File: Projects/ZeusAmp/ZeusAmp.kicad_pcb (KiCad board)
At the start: 2 copper layers, 58 parts, among them Q1 NZT660, Q11 NZT660, Q12 NZT660, Q121 NZT660, Q2 NZT660, Q21 NZT660, Q3 PZTA06, Q31 PZTA06, Q4 MJD340T4, Q41 MJD340T4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

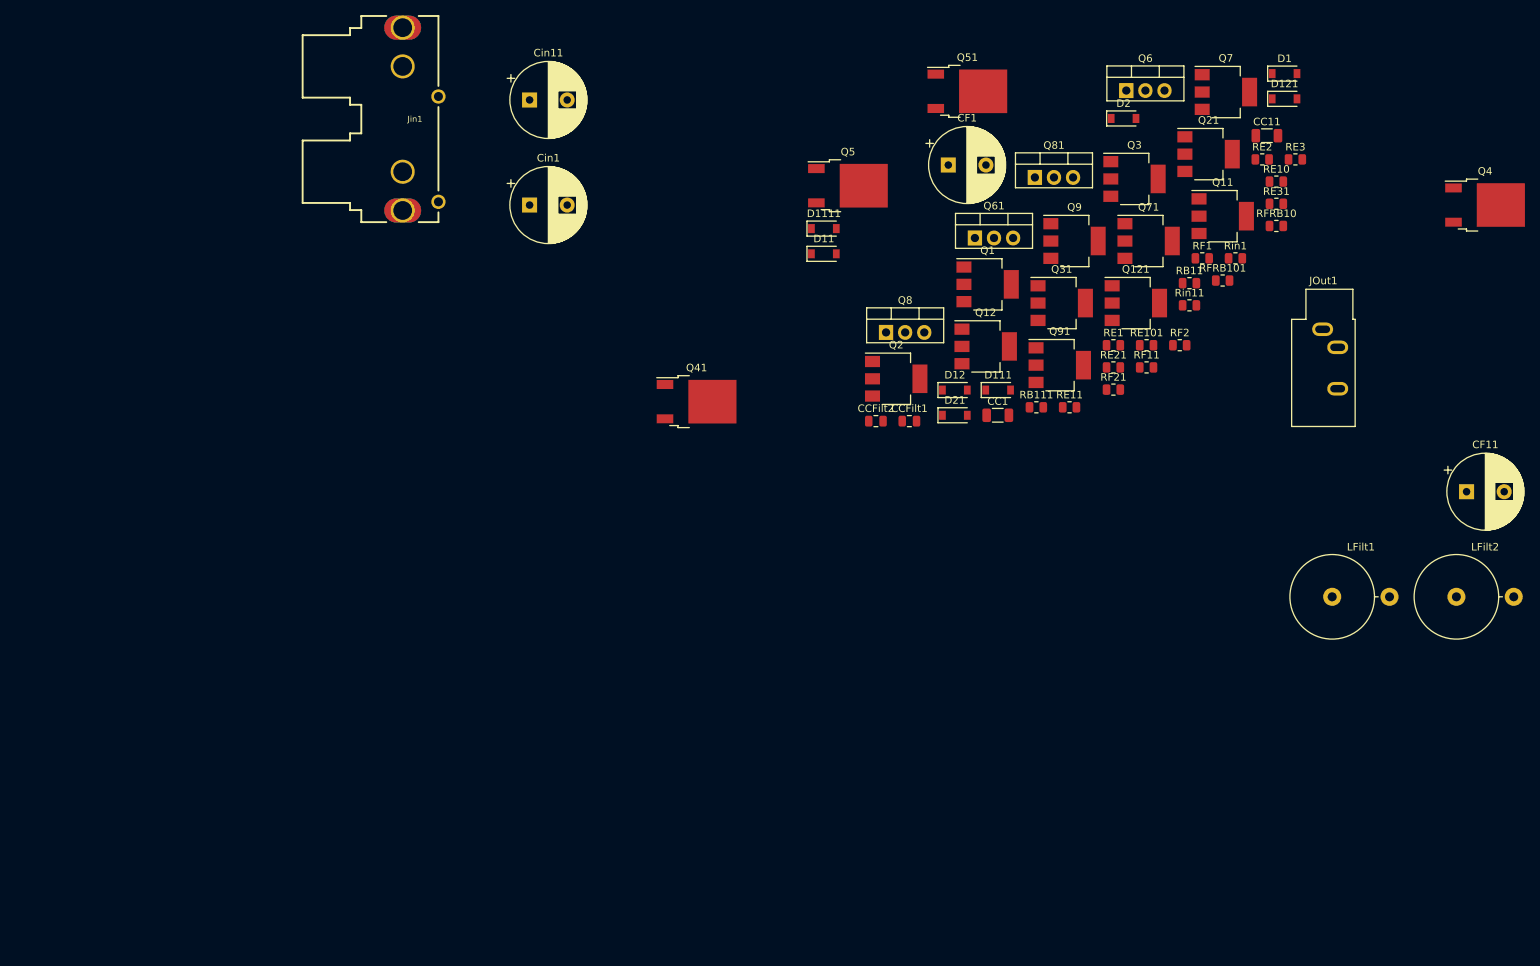
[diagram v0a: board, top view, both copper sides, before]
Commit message: completed full layout, needs volume control pot and +-15V rails
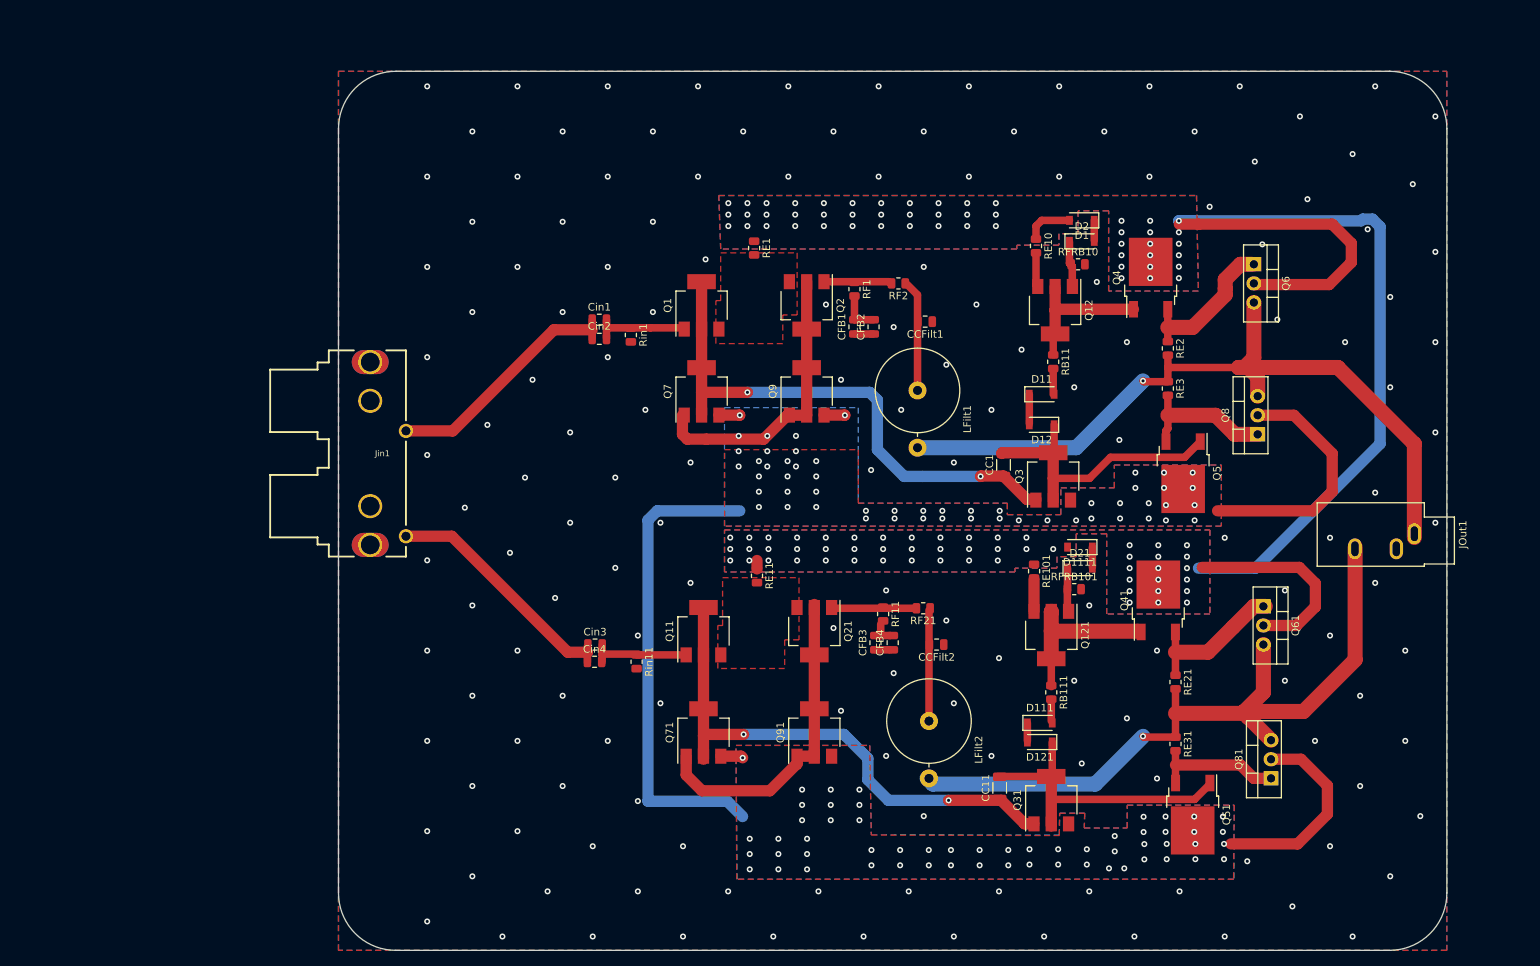
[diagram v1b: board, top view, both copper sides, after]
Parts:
- removed CF1, CF11, Cin11: 20u, Capacitor_THT:CP_Radial_D10.0mm_P5.00mm
- added CFB1: 10u, Capacitor_SMD:C_0805_2012Metric, F.Cu at (127.0, 84.8)
- added CFB2: 10u, Capacitor_SMD:C_0805_2012Metric, F.Cu at (129.5, 84.8)
- added CFB3: 10u, Capacitor_SMD:C_0805_2012Metric, F.Cu at (129.8, 126.7)
- added CFB4: 10u, Capacitor_SMD:C_0805_2012Metric, F.Cu at (132.1, 126.7)
- added Cin2: 10u, Capacitor_SMD:C_0805_2012Metric, F.Cu at (93.1, 86.4)
- added Cin3: 10u, Capacitor_SMD:C_0805_2012Metric, F.Cu at (92.5, 127.0)
- added Cin4: 10u, Capacitor_SMD:C_0805_2012Metric, F.Cu at (92.5, 129.3)
- Cin1: value 20u -> 10u; footprint Capacitor_THT:CP_Radial_D10.0mm_P5.00mm -> Capacitor_SMD:C_0805_2012Metric
- moved Q51 100.7 mm to (172.0, 149.6), turned to 270 degrees
- moved CC11 93.7 mm to (146.3, 146.1), turned to 90 degrees
- moved D121 91.5 mm to (151.6, 140.0), turned to 180 degrees
- moved Q11 88.4 mm to (106.9, 125.2), turned to 90 degrees
- moved Q71 88.1 mm to (106.9, 138.7), turned to 90 degrees
- moved Rin11 87.4 mm to (98.0, 129.3), turned to 270 degrees
- moved Q81 85.8 mm to (182.4, 144.8), turned to 90 degrees
- moved Q21 82.3 mm to (121.7, 125.2), turned to 270 degrees
- moved Rin1 81.0 mm to (97.3, 85.9), turned to 270 degrees
- moved Q7 80.2 mm to (106.7, 93.3), turned to 90 degrees
- moved RE31 73.0 mm to (169.7, 140.2), turned to 270 degrees
- moved LFilt2 72.0 mm to (136.9, 137.2), turned to 270 degrees
- moved Q41 66.8 mm to (167.4, 121.1), turned to 90 degrees
- moved Q31 66.1 mm to (153.2, 147.7), turned to 90 degrees
- moved Q61 62.2 mm to (181.4, 121.9), turned to 270 degrees
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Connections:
- net Net-(Q1-Pad3) renamed /CollectorInput
- Jin1 pad 2: Net-(Cin11-Pad1) -> Net-(Cin1-Pad1)
- Jin1 pad 4: Net-(Cin1-Pad1) -> Net-(Cin3-Pad1)
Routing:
- net /VCC: track 0.00 -> 164.3 mm, vias 0 -> 105
- net /VEE: track 0.00 -> 132.6 mm, vias 0 -> 102
- net /LeftAudioChannel: track 0.00 -> 105.4 mm, vias 0 -> 1
- net /RightAudioChannel: track 0.00 -> 100.5 mm, vias 0 -> 1
- net Net-(CC1-Pad1): track 0.00 -> 72.0 mm, vias 0 -> 2
- net Net-(CC11-Pad1): track 0.00 -> 70.8 mm, vias 0 -> 2
- net Net-(Q21-Pad2): track 0.00 -> 42.0 mm
- net Net-(CC11-Pad2): track 0.00 -> 40.2 mm
- net Net-(CC1-Pad2): track 0.00 -> 38.8 mm
- net Net-(Q2-Pad2): track 0.00 -> 38.4 mm, vias 0 -> 2
- net Net-(Cin1-Pad1): track 0.00 -> 32.8 mm
- net Net-(Cin3-Pad1): track 0.00 -> 32.6 mm
- net Net-(Q121-Pad2): track 0.00 -> 21.3 mm
- net Net-(Q4-Pad3): track 0.00 -> 20.0 mm
- net Net-(Q41-Pad3): track 0.00 -> 19.9 mm
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- added copper zone on F.Cu, net /CollectorInput
- added copper zone on B.Cu, net /VCC
- added copper zone on F.Cu, net /VCC
- added copper zone on B.Cu, net /VEE
- added copper zone on F.Cu, net /VEE
- added copper zone on B.Cu, net GND
- added copper zone on F.Cu, net GND
- added copper zone on F.Cu, net Net-(Q11-Pad3)
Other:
- board outline added: 147.3 x 116.8 mm

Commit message: First Zeus V1 completed
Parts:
- added 16VACIn1: Barrel_Jack, Connector_BarrelJack:BarrelJack_Horizontal, F.Cu at (33.0, 134.6)
- added CPower1: 1000u, Capacitor_THT:CP_Radial_D13.0mm_P5.00mm, F.Cu at (46.2, 128.8)
- added CPower11: 1000u, Capacitor_THT:CP_Radial_D13.0mm_P5.00mm, F.Cu at (45.7, 160.0)
- added CPower2: 10u, Capacitor_SMD:C_0805_2012Metric, F.Cu at (51.6, 134.9)
- added CPower22: 10u, Capacitor_Tantalum_SMD:CP_EIA-6032-28_Kemet-C, F.Cu at (55.1, 148.6)
- added CPower3: 10u, Capacitor_Tantalum_SMD:CP_EIA-6032-28_Kemet-C, F.Cu at (73.7, 133.7)
- added CPower5: 10u, Capacitor_Tantalum_SMD:CP_EIA-6032-28_Kemet-C, F.Cu at (78.7, 157.5)
- added DP1: 1N4148W, Diode_SMD:D_SOD-123, F.Cu at (43.2, 146.3)
- added DP2: 1N4148W, Diode_SMD:D_SOD-123, F.Cu at (44.5, 135.9)
- added RV1: R_POT_Dual, Potentiometer_THT:Potentiometer_Alps_RK09L_Double_Vertical, F.Cu at (85.2, 106.3)
- added U5: LM2990S-15_NOPB, Package_TO_SOT_SMD:TO-263-3_TabPin2, F.Cu at (66.0, 149.6)
- added U6: LM2937ESX-15_NOPB, Package_TO_SOT_SMD:TO-263-3_TabPin2, F.Cu at (61.4, 130.4)
- moved Jin1 33.8 mm to (30.5, 101.6)
- moved Cin4 13.0 mm to (91.4, 116.3)
- moved Rin11 13.0 mm to (97.0, 116.3)
- moved Cin3 13.0 mm to (91.5, 114.0)
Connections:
- Jin1 pad 2: Net-(Cin1-Pad1) -> Net-(Jin1-Pad2)
- Jin1 pad 4: Net-(Cin3-Pad1) -> Net-(Jin1-Pad4)
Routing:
- net /VCC: track 164.3 -> 281.6 mm, vias 105 -> 106
- net Net-(Jin1-Pad2): track 0.00 -> 55.9 mm
- net Net-(Jin1-Pad4): track 0.00 -> 52.5 mm
- net /VEE: track 132.6 -> 179.5 mm
- net Net-(CPower11-Pad2): track 0.00 -> 40.6 mm
- net /V-: track 0.00 -> 27.0 mm
- net Net-(CPower1-Pad1): track 0.00 -> 19.7 mm
- net /V+: track 0.00 -> 10.1 mm
- net Net-(Cin3-Pad2): track 13.4 -> 23.2 mm
- net Net-(Cin3-Pad1): track 32.6 -> 23.6 mm, vias 0 -> 1
- net GND: track 4.50 -> 13.5 mm, vias 159 -> 143
- net Net-(Cin1-Pad1): track 32.8 -> 24.2 mm
- net Net-(Q2-Pad2): vias 2 -> 0
- net (no net): vias 7 -> 0
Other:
- board size 147.3 x 116.8 mm -> 182.9 x 104.1 mm

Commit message: Fixed Power Supply Issue
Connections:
- 16VACIn1 pad 2: /V- -> GND
- DP1 pad 1: /V- -> /V+
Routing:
- net /V-: track 27.0 -> 0.00 mm
- net /V+: track 10.1 -> 23.8 mm

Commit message: Added Drill holes
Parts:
- added H1: MountingHole_Pad, MountingHole:MountingHole_2.2mm_M2, F.Cu at (30.5, 71.1)
- added H2: MountingHole_Pad, MountingHole:MountingHole_2.2mm_M2, F.Cu at (198.1, 71.1)
- added H3: MountingHole_Pad, MountingHole:MountingHole_2.2mm_M2, F.Cu at (198.1, 160.0)
- added H4: MountingHole_Pad, MountingHole:MountingHole_2.2mm_M2, F.Cu at (30.5, 160.0)
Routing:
- net /VCC: track 281.6 -> 271.9 mm
- net GND: vias 143 -> 139
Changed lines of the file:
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@@
     (thickness 1.6)
     (drawings 8)
-    (tracks 630)
+    (tracks 623)
     (zones 0)
-    (modules 74)
+    (modules 78)
     (nets 45)
   )
@@
   )
   (setup
-    (last_trace_width 0.5)
+    (last_trace_width 2)
     (user_trace_width 0.5)
     (user_trace_width 1)
@@
     (add_net "Net-(Q51-Pad3)")
   )
+  (module MountingHole:MountingHole_2.2mm_M2 (layer F.Cu)
+    (at 30.48 160.02)
+    (descr "Mounting Hole 2.2mm, no annular, M2")
+    (tags "mounting hole 2.2mm no annular m2")
+    (attr virtual)
+    (fp_text reference H4 (at 0 -3.2) (layer F.SilkS)
+      (effects (font (size 1 1) (thickness 0.15)))
+    )
+    (fp_text value MountingHole_Pad (at 0 3.2) (layer F.Fab)
+      (effects (font (size 1 1) (thickness 0.15)))
+    )
+    (fp_text user %R (at 0.3 0) (layer F.Fab)
+      (effects (font (size 1 1) (thickness 0.15)))
+    )
+    (fp_circle (center 0 0) (end 2.2 0) (layer Cmts.User) (width 0.15))
+    (fp_circle (center 0 0) (end 2.45 0) (layer F.CrtYd) (width 0.05))
+    (pad 1 np_thru_hole circle (at 0 0) (size 2.2 2.2) (drill 2.2) (layers *.Cu *.Mask)
+      (net 6 GND))
+  )
   (module AdditionalLibs:RCJ-2121 (layer F.Cu)
     (at 30.48 101.6)
@@
       (net 41 "Net-(Jin1-Pad2)"))
   )
+  (module MountingHole:MountingHole_2.2mm_M2 (layer F.Cu)
+    (at 198.12 160.02)
+    (descr "Mounting Hole 2.2mm, no annular, M2")
+    (tags "mounting hole 2.2mm no annular m2")
+    (attr virtual)
+    (fp_text reference H3 (at 0 -3.2) (layer F.SilkS)
+      (effects (font (size 1 1) (thickness 0.15)))
+    )
+    (fp_text value MountingHole_Pad (at 0 3.2) (layer F.Fab)
+      (effects (font (size 1 1) (thickness 0.15)))
+    )
+    (fp_text user %R (at 4.21 -2.54) (layer F.Fab)
+      (effects (font (size 1 1) (thickness 0.15)))
+    )
+    (fp_circle (center 0 0) (end 2.2 0) (layer Cmts.User) (width 0.15))
+    (fp_circle (center 0 0) (end 2.45 0) (layer F.CrtYd) (width 0.05))
+    (pad 1 np_thru_hole circle (at 0 0) (size 2.2 2.2) (drill 2.2) (layers *.Cu *.Mask)
+      (net 6 GND))
+  )
+  (module MountingHole:MountingHole_2.2mm_M2 (layer F.Cu)
+    (at 198.12 71.12)
+    (descr "Mounting Hole 2.2mm, no annular, M2")
+    (tags "mounting hole 2.2mm no annular m2")
+    (attr virtual)
+    (fp_text reference H2 (at 0 -3.2) (layer F.SilkS)
+      (effects (font (size 1 1) (thickness 0.15)))
+    )
+    (fp_text value MountingHole_Pad (at 0 3.2) (layer F.Fab)
+      (effects (font (size 1 1) (thickness 0.15)))
+    )
+    (fp_text user %R (at 0.3 0) (layer F.Fab)
+      (effects (font (size 1 1) (thickness 0.15)))
+    )
+    (fp_circle (center 0 0) (end 2.2 0) (layer Cmts.User) (width 0.15))
+    (fp_circle (center 0 0) (end 2.45 0) (layer F.CrtYd) (width 0.05))
+    (pad 1 np_thru_hole circle (at 0 0) (size 2.2 2.2) (drill 2.2) (layers *.Cu *.Mask)
+      (net 6 GND))
+  )
+  (module MountingHole:MountingHole_2.2mm_M2 (layer F.Cu)
+    (at 30.48 71.12)
+    (descr "Mounting Hole 2.2mm, no annular, M2")
+    (tags "mounting hole 2.2mm no annular m2")
+    (attr virtual)
+    (fp_text reference H1 (at 0 -3.2) (layer F.SilkS)
+      (effects (font (size 1 1) (thickness 0.15)))
+    )
+    (fp_text value MountingHole_Pad (at 0 3.2) (layer F.Fab)
+      (effects (font (size 1 1) (thickness 0.15)))
+    )
+    (fp_text user %R (at 0.3 0) (layer F.Fab)
+      (effects (font (size 1 1) (thickness 0.15)))
+    )
+    (fp_circle (center 0 0) (end 2.2 0) (layer Cmts.User) (width 0.15))
+    (fp_circle (center 0 0) (end 2.45 0) (layer F.CrtYd) (width 0.05))
+    (pad 1 np_thru_hole circle (at 0 0) (size 2.2 2.2) (drill 2.2) (layers *.Cu *.Mask)
+      (net 6 GND))
+  )
   (module Package_TO_SOT_SMD:TO-263-3_TabPin2 (layer F.Cu)
     (at 61.36 130.363 90)
@@
   (via (at 26.229999 130.5445) (size 1.6) (drill 0.8) (layers F.Cu B.Cu) (net 6))
   (via (at 26.229999 148.5445) (size 1.6) (drill 0.8) (layers F.Cu B.Cu) (net 6))
-  (via (at 26.229999 161.1445) (size 1.6) (drill 0.8) (layers F.Cu B.Cu) (net 6))
-  (via (at 31.629999 72.9445) (size 1.6) (drill 0.8) (layers F.Cu B.Cu) (net 6))
   (via (at 31.629999 85.5445) (size 1.6) (drill 0.8) (layers F.Cu B.Cu) (net 6))
   (via (at 33.429999 101.7445) (size 1.6) (drill 0.8) (layers F.Cu B.Cu) (net 6))
@@
   (via (at 179.229999 164.7445) (size 1.6) (drill 0.8) (layers F.Cu B.Cu) (net 6))
   (via (at 181.029999 148.5445) (size 1.6) (drill 0.8) (layers F.Cu B.Cu) (net 6))
-  (via (at 184.629999 74.7445) (size 1.6) (drill 0.8) (layers F.Cu B.Cu) (net 6))
   (via (at 184.629999 92.7445) (size 1.6) (drill 0.8) (layers F.Cu B.Cu) (net 6))
   (via (at 184.629999 119.7445) (size 1.6) (drill 0.8) (layers F.Cu B.Cu) (net 6))
@@
   (via (at 191.829999 98.1445) (size 1.6) (drill 0.8) (layers F.Cu B.Cu) (net 6))
   (via (at 191.829999 152.1445) (size 1.6) (drill 0.8) (layers F.Cu B.Cu) (net 6))
-  (via (at 191.829999 164.7445) (size 1.6) (drill 0.8) (layers F.Cu B.Cu) (net 6))
   (via (at 195.429999 134.1445) (size 1.6) (drill 0.8) (layers F.Cu B.Cu) (net 6))
   (via (at 197.229999 105.3445) (size 1.6) (drill 0.8) (layers F.Cu B.Cu) (net 6))
   (via (at 197.229999 117.9445) (size 1.6) (drill 0.8) (layers F.Cu B.Cu) (net 6))
   (via (at 197.229999 144.9445) (size 1.6) (drill 0.8) (layers F.Cu B.Cu) (net 6))
-  (via (at 199.029999 157.5445) (size 1.6) (drill 0.8) (layers F.Cu B.Cu) (net 6))
-  (via (at 200.829999 69.3445) (size 1.6) (drill 0.8) (layers F.Cu B.Cu) (net 6))
   (via (at 200.829999 81.9445) (size 1.6) (drill 0.8) (layers F.Cu B.Cu) (net 6))
   (via (at 200.829999 94.5445) (size 1.6) (drill 0.8) (layers F.Cu B.Cu) (net 6))
   (via (at 200.829999 126.9445) (size 1.6) (drill 0.8) (layers F.Cu B.Cu) (net 6))
+  (via (at 175.26 74.93) (size 1.6) (drill 0.8) (layers F.Cu B.Cu) (net 6))
+  (via (at 185.42 76.2) (size 1.6) (drill 0.8) (layers F.Cu B.Cu) (net 6))
   (segment (start 136.906 137.16) (end 136.906 122.428) (width 1) (layer F.Cu) (net 7))
   (segment (start 99.883 84.897) (end 104.201 84.897) (width 1) (layer F.Cu) (net 8))
@@
   (segment (start 193.04 73.66) (end 190.5 71.12) (width 2) (layer F.Cu) (net 10))
   (segment (start 190.5 71.12) (end 172.72 71.12) (width 2) (layer F.Cu) (net 10))
-  (segment (start 195.86 70.449999) (end 196.861998 71.451997) (width 2) (layer B.Cu) (net 10))
-  (segment (start 196.861998 71.451997) (end 196.861998 100.318002) (width 2) (layer B.Cu) (net 10))
-  (segment (start 194.563998 70.449999) (end 195.86 70.449999) (width 2) (layer B.Cu) (net 10))
-  (segment (start 194.338497 70.6755) (end 194.563998 70.449999) (width 2) (layer B.Cu) (net 10))
-  (segment (start 170.1165 70.6755) (end 194.338497 70.6755) (width 2) (layer B.Cu) (net 10))
-  (segment (start 196.861998 100.318002) (end 180.34 116.84) (width 2) (layer B.Cu) (net 10))
-  (segment (start 180.34 116.84) (end 172.72 116.84) (width 2) (layer B.Cu) (net 10))
-  (segment (start 170.1165 70.6755) (end 172.2755 70.6755) (width 2) (layer B.Cu) (net 10))
   (segment (start 172.72 71.12) (end 170.18 71.12) (width 2) (layer F.Cu) (net 10))
   (segment (start 63.9 136.138) (end 74.162 136.138) (width 1) (layer F.Cu) (net 10))
@@
   (segment (start 69.088 100.965) (end 96.901 73.152) (width 2) (layer B.Cu) (net 10))
   (segment (start 96.901 73.152) (end 113.538 73.152) (width 2) (layer B.Cu) (net 10))
+  (segment (start 180.34 116.84) (end 172.72 116.84) (width 2) (layer B.Cu) (net 10))
+  (segment (start 196.861998 100.318002) (end 180.34 116.84) (width 2) (layer B.Cu) (net 10))
+  (segment (start 196.861998 84.016497) (end 196.861998 100.318002) (width 2) (layer B.Cu) (net 10))
+  (segment (start 183.521001 70.6755) (end 196.861998 84.016497) (width 2) (layer B.Cu) (net 10))
+  (segment (start 170.1165 70.6755) (end 183.521001 70.6755) (width 2) (layer B.Cu) (net 10))
   (segment (start 158.876 70.612) (end 158.876 73.278) (width 1) (layer F.Cu) (net 11))
   (segment (start 155.576 73.406) (end 155.576 76.328) (width 1) (layer F.Cu) (net 12))

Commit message: added switch
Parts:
- added S1: 100SP1T1B4M2QE, AdditionalLibs:SW_100SP1T1B4M2QE, F.Cu at (27.9, 144.1)
- moved 16VACIn1 10.2 mm to (31.8, 124.5)
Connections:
- 16VACIn1 pad 1: /V+ -> Net-(16VACIn1-Pad1)
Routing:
- net Net-(16VACIn1-Pad1): track 0.00 -> 21.9 mm
- net /V+: track 23.8 -> 27.1 mm
- net GND: vias 139 -> 132
